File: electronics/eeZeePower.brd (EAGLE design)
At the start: 25.9 x 12.7 mm, 11 parts

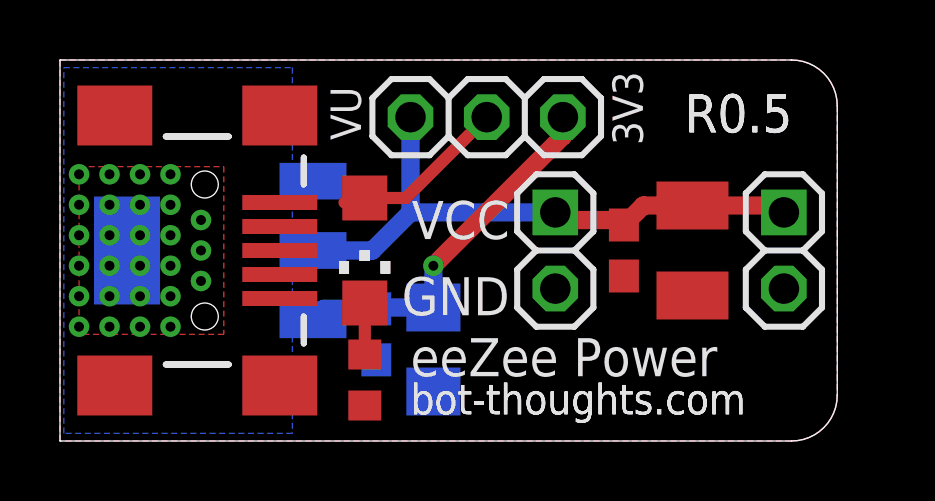
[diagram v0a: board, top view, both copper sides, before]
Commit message: replaced logo, moved power pin headers, changed layout of passives, added help url
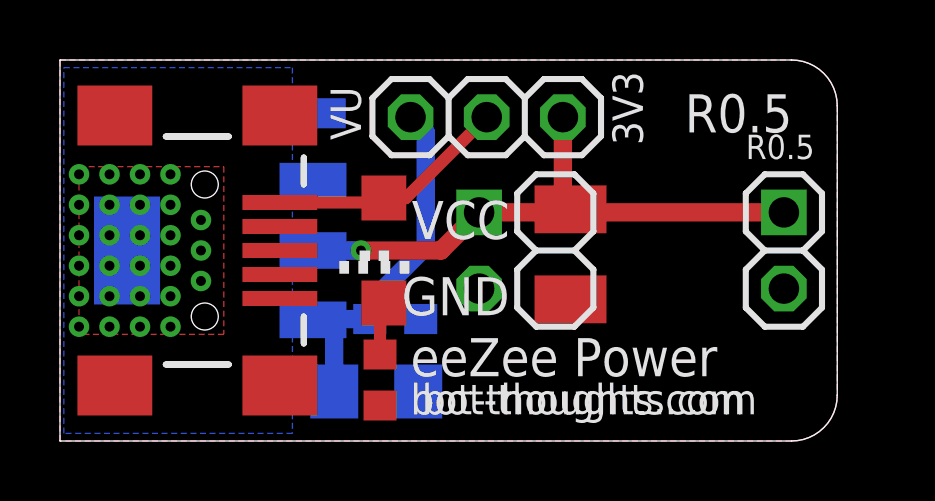
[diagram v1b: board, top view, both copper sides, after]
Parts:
- added U$3: BOT-THOUGHTS-LOGO-MD, bt:BTLOGOM
- moved C3 11.6 mm to (8.13, 10.9), flipped to the bottom, turned to 180 degrees
- moved C4 4.07 mm to (17.0, 6.22)
- moved JP3 2.54 mm to (14.0, 6.35), flipped to the bottom
- moved C1 2.36 mm to (10.5, 1.65), turned to 180 degrees
- moved C2 0.81 mm to (11.2, 4.06), turned to 180 degrees
- moved LED1 0.63 mm to (10.8, 6.35)
- moved R1 0.51 mm to (10.7, 2.03)
- turned JP10 to 0 degrees
- flipped JP4 to the bottom
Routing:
- net VBUS: track 5.87 -> 8.08 mm
- net VOUT: track 20.0 -> 20.4 mm, vias 27 -> 28
- net VIN: track 12.3 -> 12.6 mm, vias 1 -> 0
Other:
- board text added: "CC-BY-SA"
- board text added: "is.gd/MTPmIU"
